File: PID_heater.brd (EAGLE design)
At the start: 32 x 68.6 mm, 15 parts, among them T1 BT136

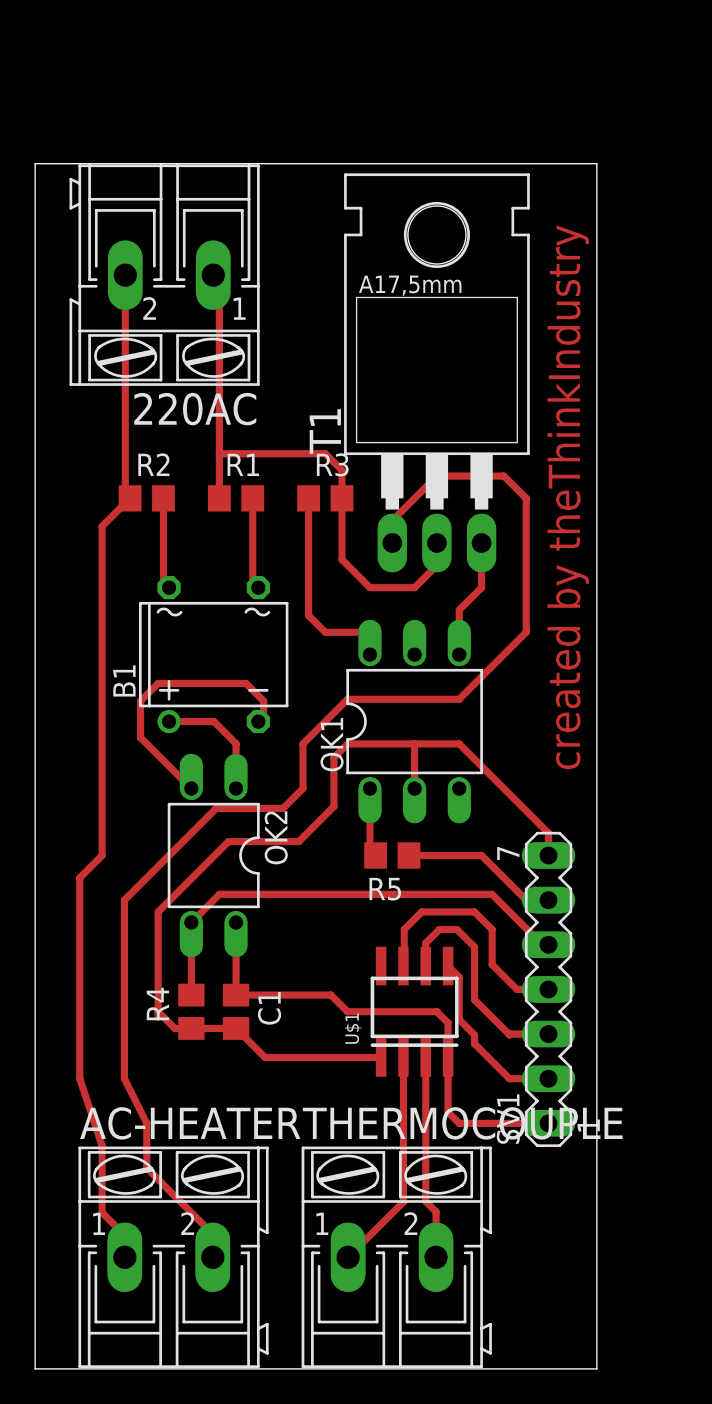
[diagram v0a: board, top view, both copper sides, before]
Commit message: Wires  width changed
pin Names and TheThinkIndustry Logos Added
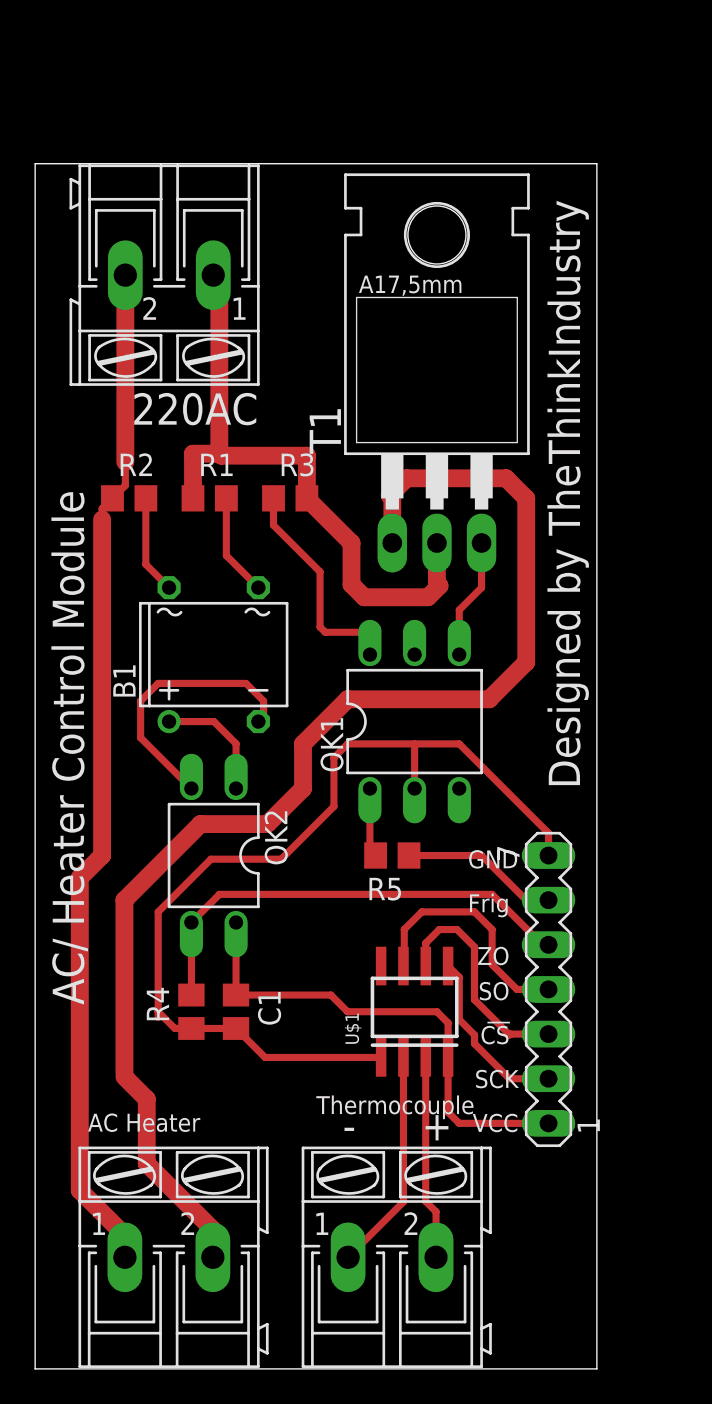
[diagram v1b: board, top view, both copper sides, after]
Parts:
- moved R3 2.00 mm to (14.5, 49.5)
- moved R1 1.50 mm to (9.93, 49.5)
- moved R2 1.00 mm to (5.35, 49.5)
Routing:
- net N$12: track 70.9 -> 77.0 mm
- net N$2: track 33.2 -> 35.8 mm
- net N$1: track 11.8 -> 12.7 mm
- net N$4: track 5.21 -> 5.83 mm
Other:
- board text added: "+"
- board text added: "-"
- board text added: "AC Heater"
- board text added: "AC/ Heater Control Module"
- board text added: "CS"
- board text added: "Designed by TheThinkIndustry"
- board text added: "Frig"
- board text added: "GND"
- board text added: "SCK"
- board text added: "SO"
- board text added: "The Think Industry"
- board text added: "Thermocouple"
- board text added: "VCC"
- board text added: "ZO"
- board text added: "__"
- board text removed: "created by theThinkIndustry"
